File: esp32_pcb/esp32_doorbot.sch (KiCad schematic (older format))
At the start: 17 parts, among them J1 Conn_01x07_Male, J2 Conn_01x02_Female, J3 Barrel_Jack, J4 WROOM32_1, J5 WROOM32_2, Q1 2N7002E, U1 L7805, U2 74LVC2T45DC

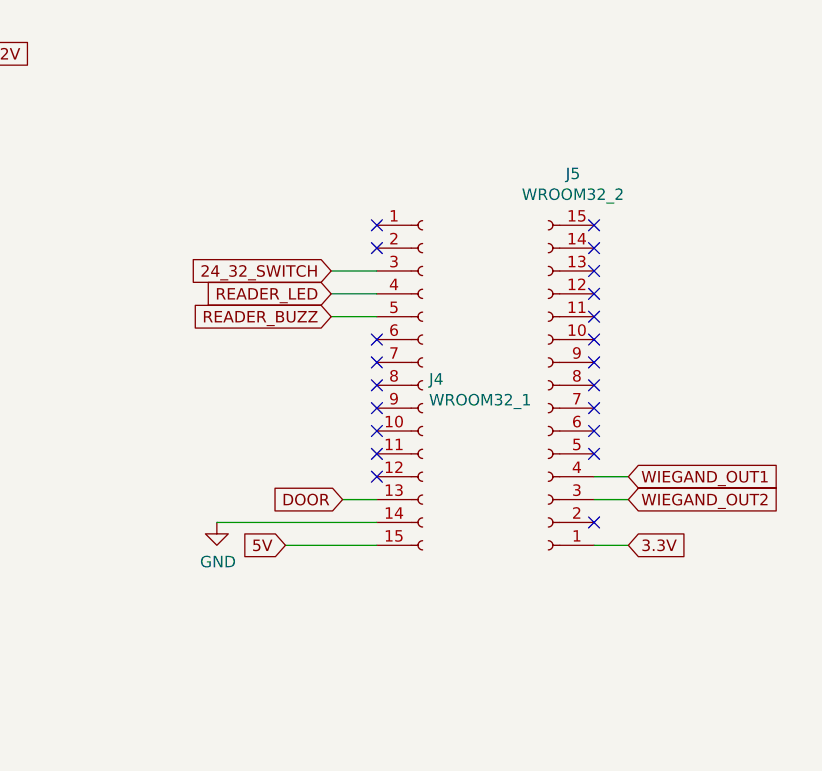
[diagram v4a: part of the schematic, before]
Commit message: Use larger components. Correct pinout and spacing
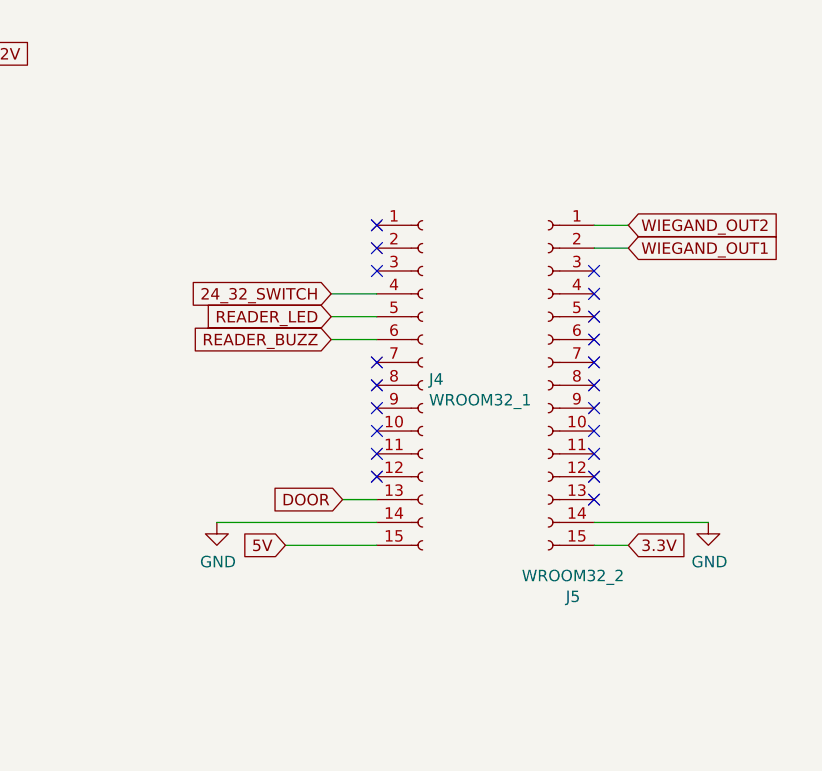
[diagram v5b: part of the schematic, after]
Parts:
- D1: footprint LEDs:LED_0603 -> LEDs:LED-1206; Digikey # SML-D12U1WT86TR-ND -> 1516-1073-2-N
- D2: footprint LEDs:LED_0603 -> LEDs:LED-1206; Digikey # SML-D12U1WT86TR-ND -> 1516-1072-2-ND
- D3: footprint Diodes_SMD:SOD-523 -> SMD_Packages:SMD-1206_Pol; Digikey # 31-SDM20U30Q-7TR-ND -> 478-7805-2-ND
- D4: footprint LEDs:LED_0603 -> LEDs:LED-1206; Digikey # SML-D12U1WT86TR-ND -> 1516-1076-2-ND
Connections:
- net 24_32_SWITCH: now also J4.4 (Pin_4); no longer J4.3 (Pin_3)
- net 3.3V: now also J5.15 (Pin_15); no longer J5.1 (Pin_1)
- net GND: now also J5.14 (Pin_14)
- net READER_BUZZ: now also J4.6 (Pin_6); no longer J4.5 (Pin_5)
- net READER_LED: now also J4.5 (Pin_5); no longer J4.4 (Pin_4)
- net WIEGAND_OUT1: now also J5.2 (Pin_2); no longer J5.4 (Pin_4)
- net WIEGAND_OUT2: now also J5.1 (Pin_1); no longer J5.3 (Pin_3)
- no-connect marks 21 -> 20
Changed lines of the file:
@@
 F 0 "D3" V 1304 5230 50  0000 L CNN
 F 1 "D_Schottky" V 1395 5230 50  0000 L CNN
-F 2 "Diodes_SMD:SOD-523" H 1350 5150 50  0001 C CNN
+F 2 "SMD_Packages:SMD-1206_Pol" H 1350 5150 50  0001 C CNN
 F 3 "~" H 1350 5150 50  0001 C CNN
-F 4 "31-SDM20U30Q-7TR-ND" V 1350 5150 50  0001 C CNN "Digikey #"
+F 4 "478-7805-2-ND" V 1350 5150 50  0001 C CNN "Digikey #"
 	1    1350 5150
 	0    1    1    0
@@
 Text GLabel 7800 3300 0    50   Input ~ 0
 DOOR
-Text GLabel 9050 3200 2    50   Input ~ 0
-WIEGAND_OUT1
 $Comp
 L Regulator_Linear:L7805 U1
@@
 F 0 "D4" V 5539 2982 50  0000 R CNN
 F 1 "LED" V 5448 2982 50  0000 R CNN
-F 2 "LEDs:LED_0603" H 5500 3100 50  0001 C CNN
+F 2 "LEDs:LED-1206" H 5500 3100 50  0001 C CNN
 F 3 "~" H 5500 3100 50  0001 C CNN
-F 4 "SML-D12U1WT86TR-ND" V 5500 3100 50  0001 C CNN "Digikey #"
+F 4 "1516-1076-2-ND" V 5500 3100 50  0001 C CNN "Digikey #"
 	1    5500 3100
 	0    -1   -1   0
@@
 F 0 "D2" V 1239 5682 50  0000 R CNN
 F 1 "LED" V 1148 5682 50  0000 R CNN
-F 2 "LEDs:LED_0603" H 1200 5800 50  0001 C CNN
+F 2 "LEDs:LED-1206" H 1200 5800 50  0001 C CNN
 F 3 "~" H 1200 5800 50  0001 C CNN
-F 4 "SML-D12U1WT86TR-ND" V 1200 5800 50  0001 C CNN "Digikey #"
+F 4 "1516-1072-2-ND" V 1200 5800 50  0001 C CNN "Digikey #"
 	1    1200 5800
 	0    -1   -1   0
@@
 Wire Wire Line
 	5250 6400 5250 6150
-Text GLabel 7750 2400 0    50   Input ~ 0
+Text GLabel 7750 2500 0    50   Input ~ 0
 READER_LED
-Text GLabel 7750 2500 0    50   Input ~ 0
+Text GLabel 7750 2600 0    50   Input ~ 0
 READER_BUZZ
 Text GLabel 3550 1250 0    50   Input ~ 0
@@
 F 0 "D1" V 1239 1132 50  0000 R CNN
 F 1 "LED" V 1148 1132 50  0000 R CNN
-F 2 "LEDs:LED_0603" H 1200 1250 50  0001 C CNN
+F 2 "LEDs:LED-1206" H 1200 1250 50  0001 C CNN
 F 3 "~" H 1200 1250 50  0001 C CNN
-F 4 "SML-D12U1WT86TR-ND" V 1200 1250 50  0001 C CNN "Digikey #"
+F 4 "1516-1073-2-N" V 1200 1250 50  0001 C CNN "Digikey #"
 	1    1200 1250
 	0    -1   -1   0
@@
 Text GLabel 7550 3500 0    50   Input ~ 0
 5V
-Text GLabel 9050 3300 2    50   Input ~ 0
-WIEGAND_OUT2
 $Comp
 L Connector:Conn_01x15_Female J4
@@
 F 3 "~" H 8700 2800 50  0001 C CNN
 	1    8700 2800
-	-1   0    0    1
+	-1   0    0    -1
 $EndComp
 Wire Wire Line
@@
 	7800 3300 7950 3300
 Wire Wire Line
-	9050 3200 8900 3200
-Wire Wire Line
-	8900 3300 9050 3300
-Text GLabel 9050 3500 2    50   Input ~ 0
-3.3V
+	9050 2200 8900 2200
+Wire Wire Line
+	8900 2100 9050 2100
 Wire Wire Line
 	8900 3500 9050 3500
-Text GLabel 7750 2300 0    50   Input ~ 0
+Text GLabel 7750 2400 0    50   Input ~ 0
 24_32_SWITCH
 NoConn ~ 7950 3000
@@
 NoConn ~ 7950 2800
 NoConn ~ 7950 2700
-NoConn ~ 7950 2600
 NoConn ~ 7950 2200
 NoConn ~ 7950 2100
-NoConn ~ 8900 2100
-NoConn ~ 8900 2200
-NoConn ~ 8900 2300
-NoConn ~ 8900 2400
-NoConn ~ 8900 2500
-NoConn ~ 8900 2600
-NoConn ~ 8900 2700
-NoConn ~ 8900 2800
-NoConn ~ 8900 2900
-NoConn ~ 8900 3000
-NoConn ~ 8900 3400
 NoConn ~ 7950 3100
 NoConn ~ 7950 3200
+Wire Wire Line
+	7750 2400 7950 2400
+Wire Wire Line
+	7750 2500 7950 2500
+Wire Wire Line
+	7750 2600 7950 2600
+NoConn ~ 7950 2300
+Wire Wire Line
+	8900 3400 9400 3400
+$Comp
+L power:GND #PWR0110
+U 1 1 60842CA7
+P 9400 3400
+F 0 "#PWR0110" H 9400 3150 50  0001 C CNN
+F 1 "GND" H 9405 3227 50  0000 C CNN
+F 2 "" H 9400 3400 50  0001 C CNN
+F 3 "" H 9400 3400 50  0001 C CNN
+	1    9400 3400
+	1    0    0    -1
+$EndComp
+Text GLabel 9050 3500 2    50   Input ~ 0
+3.3V
+Text GLabel 9050 2100 2    50   Input ~ 0
+WIEGAND_OUT2
+Text GLabel 9050 2200 2    50   Input ~ 0
+WIEGAND_OUT1
+NoConn ~ 8900 3300
+NoConn ~ 8900 3200
 NoConn ~ 8900 3100
-Wire Wire Line
-	7750 2300 7950 2300
-Wire Wire Line
-	7750 2400 7950 2400
-Wire Wire Line
-	7750 2500 7950 2500
+NoConn ~ 8900 3000
+NoConn ~ 8900 2900
+NoConn ~ 8900 2800
+NoConn ~ 8900 2700
+NoConn ~ 8900 2600
+NoConn ~ 8900 2500
+NoConn ~ 8900 2400
+NoConn ~ 8900 2300
 $EndSCHEMATC

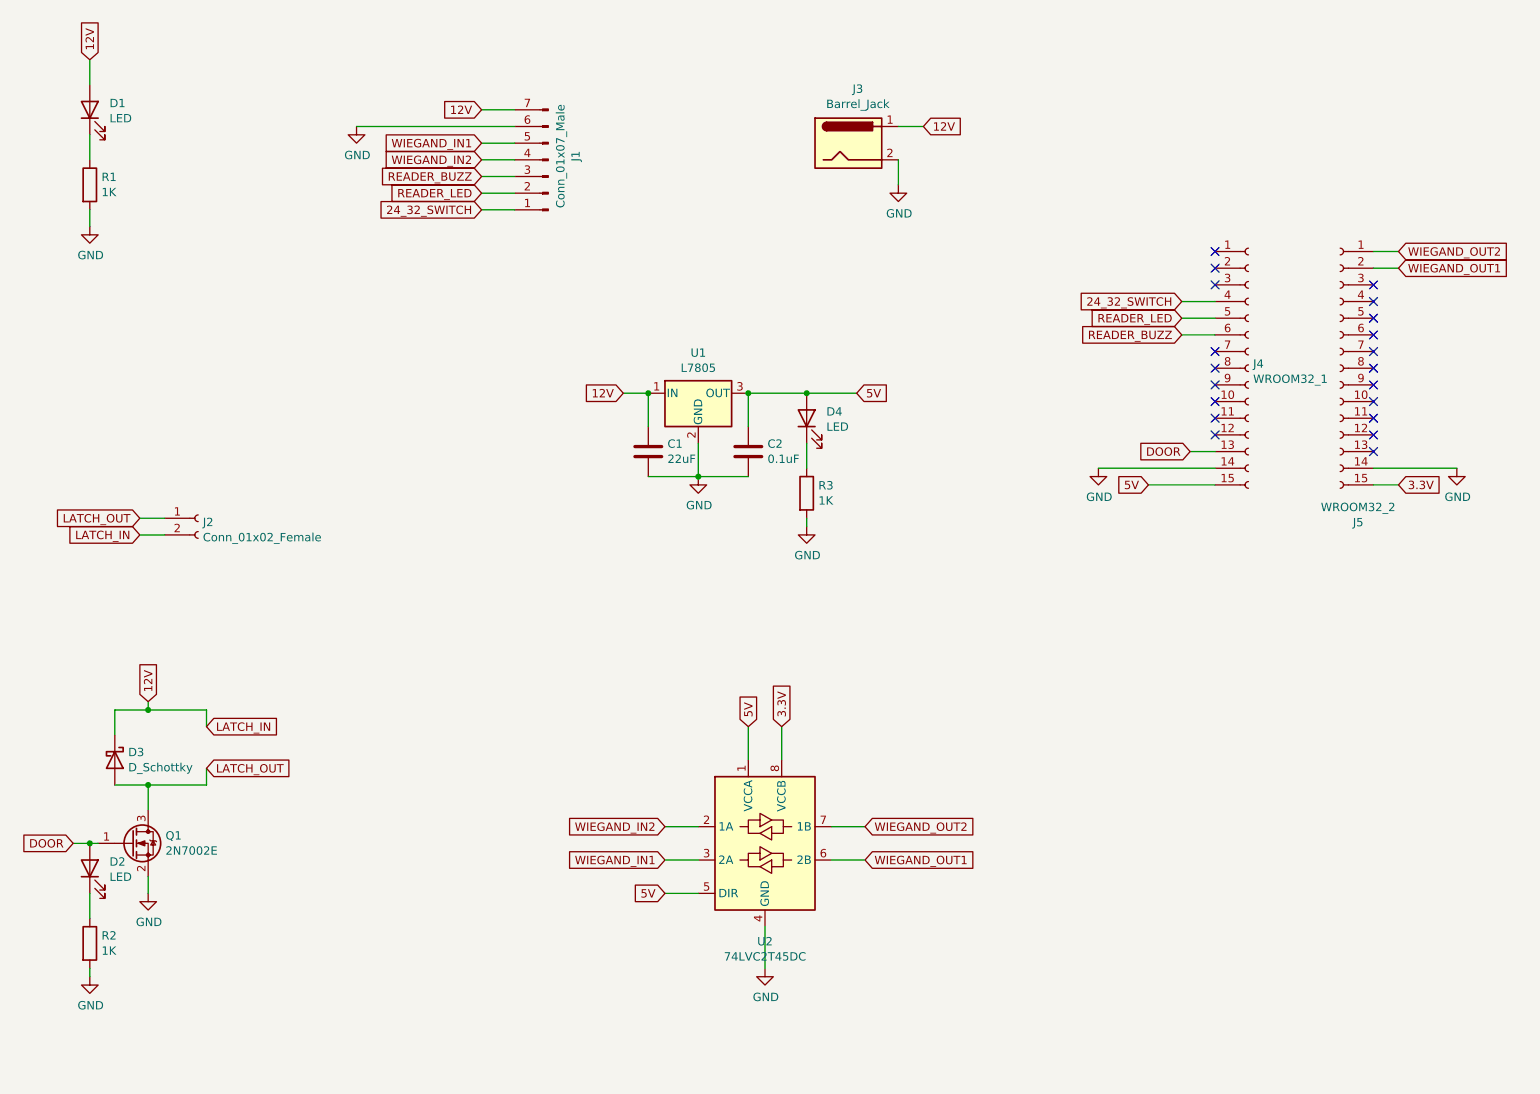
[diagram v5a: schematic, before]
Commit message: Switch to voltage divider instead of logic level converter
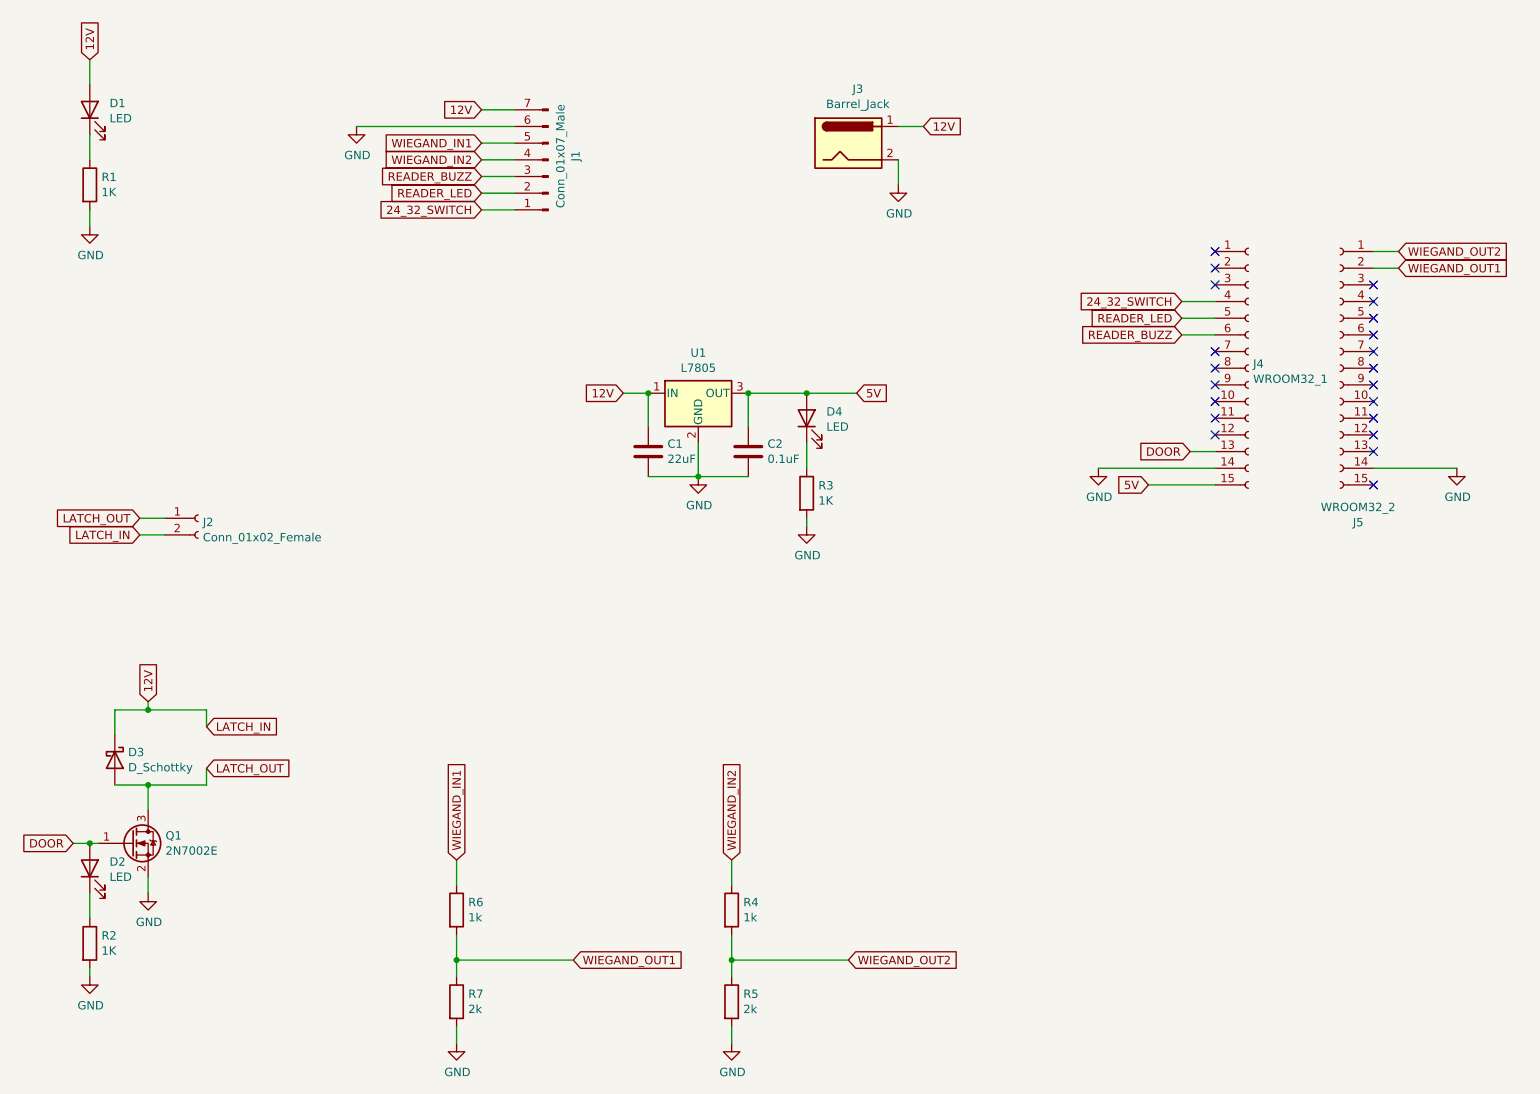
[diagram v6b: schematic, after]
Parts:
- removed U2: 74LVC2T45DC, tinkerforge-kicad:VSSOP8, symbol Logic_LevelTranslator:74LVC2T45DC
- added R4, R6: 1k, Resistors_SMD:R_1210, symbol Device:R
- added R5, R7: 2k, Resistors_SMD:R_1210, symbol Device:R
- R1, R2, R3: Digikey # 2019-RK73B2ETTD102JTR-ND -> RMCF1210FT1K00
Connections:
- net GND: now also R5.2, R7.2
- net WIEGAND_IN1: now also R6.1
- net WIEGAND_IN2: now also R4.1
- net WIEGAND_OUT1: now also R6.2, R7.1
- net WIEGAND_OUT2: now also R4.2, R5.1
- net 3.3V: no longer names the net of J5.15 (Pin_15)
- no-connect marks 20 -> 21
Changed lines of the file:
@@
 F 2 "Resistors_SMD:R_1210" V 5430 3550 50  0001 C CNN
 F 3 "~" H 5500 3550 50  0001 C CNN
-F 4 "2019-RK73B2ETTD102JTR-ND" H 5500 3550 50  0001 C CNN "Digikey #"
+F 4 "RMCF1210FT1K00" H 5500 3550 50  0001 C CNN "Digikey #"
 	1    5500 3550
 	1    0    0    -1
@@
 F 2 "Resistors_SMD:R_1210" V 1130 6250 50  0001 C CNN
 F 3 "~" H 1200 6250 50  0001 C CNN
-F 4 "2019-RK73B2ETTD102JTR-ND" H 1200 6250 50  0001 C CNN "Digikey #"
+F 4 "RMCF1210FT1K00" H 1200 6250 50  0001 C CNN "Digikey #"
 	1    1200 6250
 	1    0    0    -1
@@
 Wire Wire Line
 	1200 5650 1250 5650
-$Comp
-L Logic_LevelTranslator:74LVC2T45DC U2
-U 1 1 6061B908
-P 5250 5650
-F 0 "U2" H 5250 5061 50  0000 C CNN
-F 1 "74LVC2T45DC" H 5250 4970 50  0000 C CNN
-F 2 "tinkerforge-kicad:VSSOP8" H 5250 4800 50  0001 C CNN
-F 3 "https://assets.nexperia.com/documents/data-sheet/74LVC_LVCH2T45.pdf" H 5500 5400 50  0001 C CNN
-F 4 "1727-4578-2-ND" H 5250 5650 50  0001 C CNN "Digikey #"
-	1    5250 5650
-	1    0    0    -1
-$EndComp
-Text GLabel 5150 4950 1    50   Input ~ 0
-5V
-Text GLabel 5350 4950 1    50   Input ~ 0
-3.3V
-Wire Wire Line
-	5150 4950 5150 5150
-Wire Wire Line
-	5350 5150 5350 4950
-Text GLabel 5850 5750 2    50   Input ~ 0
+Text GLabel 4100 6350 2    50   Input ~ 0
 WIEGAND_OUT1
-Text GLabel 5850 5550 2    50   Input ~ 0
+Text GLabel 5750 6350 2    50   Input ~ 0
 WIEGAND_OUT2
-Wire Wire Line
-	5650 5550 5850 5550
-Wire Wire Line
-	5650 5750 5850 5750
-Text GLabel 4650 5750 0    50   Input ~ 0
+Text GLabel 3400 5750 1    50   Input ~ 0
 WIEGAND_IN1
-Text GLabel 4650 5550 0    50   Input ~ 0
+Text GLabel 5050 5750 1    50   Input ~ 0
 WIEGAND_IN2
-Text GLabel 4650 5950 0    50   Input ~ 0
-5V
-Wire Wire Line
-	4650 5950 4850 5950
-Wire Wire Line
-	4650 5750 4850 5750
-Wire Wire Line
-	4650 5550 4850 5550
-$Comp
-L power:GND #PWR0108
-U 1 1 6062830E
-P 5250 6400
-F 0 "#PWR0108" H 5250 6150 50  0001 C CNN
-F 1 "GND" H 5255 6227 50  0000 C CNN
-F 2 "" H 5250 6400 50  0001 C CNN
-F 3 "" H 5250 6400 50  0001 C CNN
-	1    5250 6400
-	1    0    0    -1
-$EndComp
-Wire Wire Line
-	5250 6400 5250 6150
 Text GLabel 7750 2500 0    50   Input ~ 0
 READER_LED
@@
 F 2 "Resistors_SMD:R_1210" V 1130 1700 50  0001 C CNN
 F 3 "~" H 1200 1700 50  0001 C CNN
-F 4 "2019-RK73B2ETTD102JTR-ND" H 1200 1700 50  0001 C CNN "Digikey #"
+F 4 "RMCF1210FT1K00" H 1200 1700 50  0001 C CNN "Digikey #"
 	1    1200 1700
 	1    0    0    -1
@@
 Wire Wire Line
 	8900 2100 9050 2100
-Wire Wire Line
-	8900 3500 9050 3500
 Text GLabel 7750 2400 0    50   Input ~ 0
 24_32_SWITCH
@@
 	1    0    0    -1
 $EndComp
-Text GLabel 9050 3500 2    50   Input ~ 0
-3.3V
 Text GLabel 9050 2100 2    50   Input ~ 0
 WIEGAND_OUT2
@@
 NoConn ~ 8900 2400
 NoConn ~ 8900 2300
+NoConn ~ 8900 3500
+$Comp
+L Device:R R4
+U 1 1 60E15F7D
+P 5050 6050
+F 0 "R4" H 5120 6096 50  0000 L CNN
+F 1 "1k" H 5120 6005 50  0000 L CNN
+F 2 "Resistors_SMD:R_1210" V 4980 6050 50  0001 C CNN
+F 3 "~" H 5050 6050 50  0001 C CNN
+F 4 "RMCF1210FT1K00" H 5050 6050 50  0001 C CNN "Digikey #"
+	1    5050 6050
+	1    0    0    -1
+$EndComp
+$Comp
+L Device:R R5
+U 1 1 60E1628B
+P 5050 6600
+F 0 "R5" H 5120 6646 50  0000 L CNN
+F 1 "2k" H 5120 6555 50  0000 L CNN
+F 2 "Resistors_SMD:R_1210" V 4980 6600 50  0001 C CNN
+F 3 "~" H 5050 6600 50  0001 C CNN
+F 4 "P2.0KVTR-ND" H 5050 6600 50  0001 C CNN "Digikey #"
+	1    5050 6600
+	1    0    0    -1
+$EndComp
+$Comp
+L power:GND #PWR0108
+U 1 1 60E16820
+P 5050 6850
+F 0 "#PWR0108" H 5050 6600 50  0001 C CNN
+F 1 "GND" H 5055 6677 50  0000 C CNN
+F 2 "" H 5050 6850 50  0001 C CNN
+F 3 "" H 5050 6850 50  0001 C CNN
+	1    5050 6850
+	1    0    0    -1
+$EndComp
+Wire Wire Line
+	5050 6200 5050 6350
+Wire Wire Line
+	5050 6750 5050 6850
+Connection ~ 5050 6350
+Wire Wire Line
+	5050 6350 5050 6450
+Wire Wire Line
+	5050 6350 5750 6350
+Wire Wire Line
+	5050 5750 5050 5900
+$Comp
+L Device:R R6
+U 1 1 60E258D5
+P 3400 6050
+F 0 "R6" H 3470 6096 50  0000 L CNN
+F 1 "1k" H 3470 6005 50  0000 L CNN
+F 2 "Resistors_SMD:R_1210" V 3330 6050 50  0001 C CNN
+F 3 "~" H 3400 6050 50  0001 C CNN
+F 4 "RMCF1210FT1K00" H 3400 6050 50  0001 C CNN "Digikey #"
+	1    3400 6050
+	1    0    0    -1
+$EndComp
+$Comp
+L Device:R R7
+U 1 1 60E258DC
+P 3400 6600
+F 0 "R7" H 3470 6646 50  0000 L CNN
+F 1 "2k" H 3470 6555 50  0000 L CNN
+F 2 "Resistors_SMD:R_1210" V 3330 6600 50  0001 C CNN
+F 3 "~" H 3400 6600 50  0001 C CNN
+F 4 "P2.0KVTR-ND" H 3400 6600 50  0001 C CNN "Digikey #"
+	1    3400 6600
+	1    0    0    -1
+$EndComp
+$Comp
+L power:GND #PWR0111
+U 1 1 60E258E2
+P 3400 6850
+F 0 "#PWR0111" H 3400 6600 50  0001 C CNN
+F 1 "GND" H 3405 6677 50  0000 C CNN
+F 2 "" H 3400 6850 50  0001 C CNN
+F 3 "" H 3400 6850 50  0001 C CNN
+	1    3400 6850
+	1    0    0    -1
+$EndComp
+Wire Wire Line
+	3400 6200 3400 6350
+Wire Wire Line
+	3400 6750 3400 6850
+Connection ~ 3400 6350
+Wire Wire Line
+	3400 6350 3400 6450
+Wire Wire Line
+	3400 6350 4100 6350
+Wire Wire Line
+	3400 5750 3400 5900
 $EndSCHEMATC

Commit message: Voltage dividers
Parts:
- C2: Digikey # (none) -> 478-1529-2-ND; Digkey # 478-1529-2-ND -> (none)
- J3: Digikey # (none) -> ED2561-ND
- U1: Digikey # NCV7805BDTRKGOSCT-ND -> 497-7255-2-ND
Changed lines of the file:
@@
 F 2 "TO_SOT_Packages_SMD:TO-252-2Lead" H 4875 2800 50  0001 L CIN
 F 3 "http://www.st.com/content/ccc/resource/technical/document/datasheet/41/4f/b3/b0/12/d4/47/88/CD00000444.pdf/files/CD00000444.pdf/jcr:content/translations/en.CD00000444.pdf" H 4850 2900 50  0001 C CNN
-F 4 "NCV7805BDTRKGOSCT-ND" H 4850 2950 50  0001 C CNN "Digikey #"
+F 4 "497-7255-2-ND" H 4850 2950 50  0001 C CNN "Digikey #"
 	1    4850 2950
 	1    0    0    -1
@@
 F 4 "1276-1771-2-ND" H 4550 3300 50  0001 C CNN "Digikey #"
 	1    4550 3300
-	1    0    0    -1
-$EndComp
-$Comp
-L Device:C C2
-U 1 1 60607F53
-P 5150 3300
-F 0 "C2" H 5265 3346 50  0000 L CNN
-F 1 "0.1uF" H 5265 3255 50  0000 L CNN
-F 2 "Capacitors_SMD:C_1206" H 5188 3150 50  0001 C CNN
-F 3 "~" H 5150 3300 50  0001 C CNN
-F 4 "478-1529-2-ND" H 5150 3300 50  0001 C CNN "Digkey #"
-	1    5150 3300
 	1    0    0    -1
 $EndComp
@@
 F 2 "Terminal_Blocks:TerminalBlock_Pheonix_MKDS1.5-2pol" H 5800 1410 50  0001 C CNN
 F 3 "~" H 5800 1410 50  0001 C CNN
+F 4 "ED2561-ND" H 5750 1450 50  0001 C CNN "Digikey #"
 	1    5750 1450
 	1    0    0    -1
@@
 Wire Wire Line
 	3400 5750 3400 5900
+$Comp
+L Device:C C2
+U 1 1 60E33917
+P 5150 3300
+F 0 "C2" H 5265 3346 50  0000 L CNN
+F 1 "0.1uF" H 5265 3255 50  0000 L CNN
+F 2 "Capacitors_SMD:C_1206" H 5188 3150 50  0001 C CNN
+F 3 "~" H 5150 3300 50  0001 C CNN
+F 4 "478-1529-2-ND" H 5150 3300 50  0001 C CNN "Digikey #"
+	1    5150 3300
+	1    0    0    -1
+$EndComp
 $EndSCHEMATC

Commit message: Even more pinout corrections
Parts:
- removed Q1: 2N7002E, TO_SOT_Packages_SMD:SOT-223, symbol Transistor_FET:2N7002E
- added Q1: ZXMP4A16G, TO_SOT_Packages_SMD:SOT-223, symbol Transistor_FET:ZXMP4A16G
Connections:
- net DOOR: now also Q1.1 (G)
- net GND: now also Q1.3 (S)
- net LATCH_OUT: now also Q1.2 (D)
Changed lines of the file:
@@
 $EndDescr
-$Comp
-L Transistor_FET:2N7002E Q1
-U 1 1 603A6F1F
-P 1450 5650
-F 0 "Q1" H 1654 5696 50  0000 L CNN
-F 1 "2N7002E" H 1654 5605 50  0000 L CNN
-F 2 "TO_SOT_Packages_SMD:SOT-223" H 1650 5575 50  0001 L CIN
-F 3 "http://www.diodes.com/assets/Datasheets/ds30376.pdf" H 1450 5650 50  0001 L CNN
-F 4 "ZVN4206GVTR-ND" H 1450 5650 50  0001 C CNN "Digikey #"
-	1    1450 5650
-	1    0    0    -1
-$EndComp
 $Comp
 L power:GND #PWR0101
@@
 	1    0    0    -1
 $EndComp
+$Comp
+L Transistor_FET:ZXMP4A16G Q1
+U 1 1 61512B24
+P 1450 5650
+F 0 "Q1" H 1654 5696 50  0000 L CNN
+F 1 "ZXMP4A16G" H 1654 5605 50  0000 L CNN
+F 2 "TO_SOT_Packages_SMD:SOT-223" H 1650 5575 50  0001 L CIN
+F 3 "https://www.diodes.com/assets/Datasheets/ZXMP4A16G.pdf" H 1450 5650 50  0001 L CNN
+F 4 "ZVN4206GVTR-ND" H 1450 5650 50  0001 C CNN "Digikey #"
+	1    1450 5650
+	1    0    0    -1
+$EndComp
